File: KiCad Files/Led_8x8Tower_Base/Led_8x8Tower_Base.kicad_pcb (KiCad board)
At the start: 2 copper layers, 160 x 152 mm, 0 parts

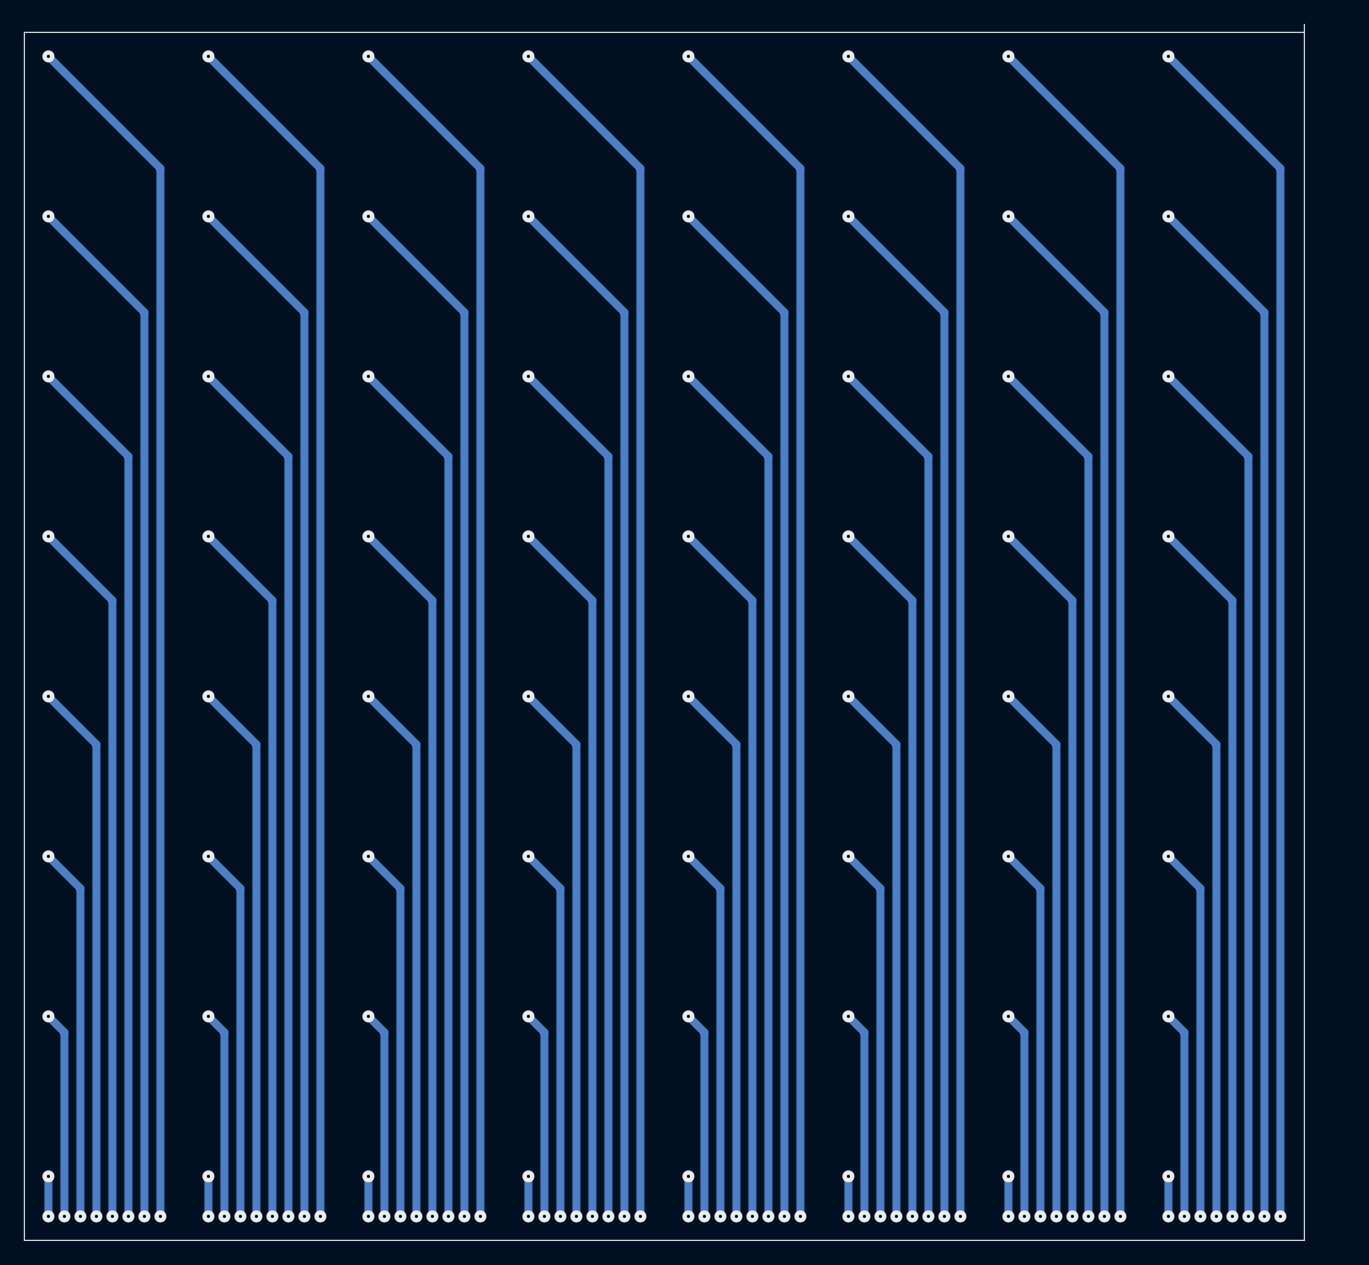
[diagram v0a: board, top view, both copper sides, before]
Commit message: Parellel processing testing files and New circuit designes  uploaded
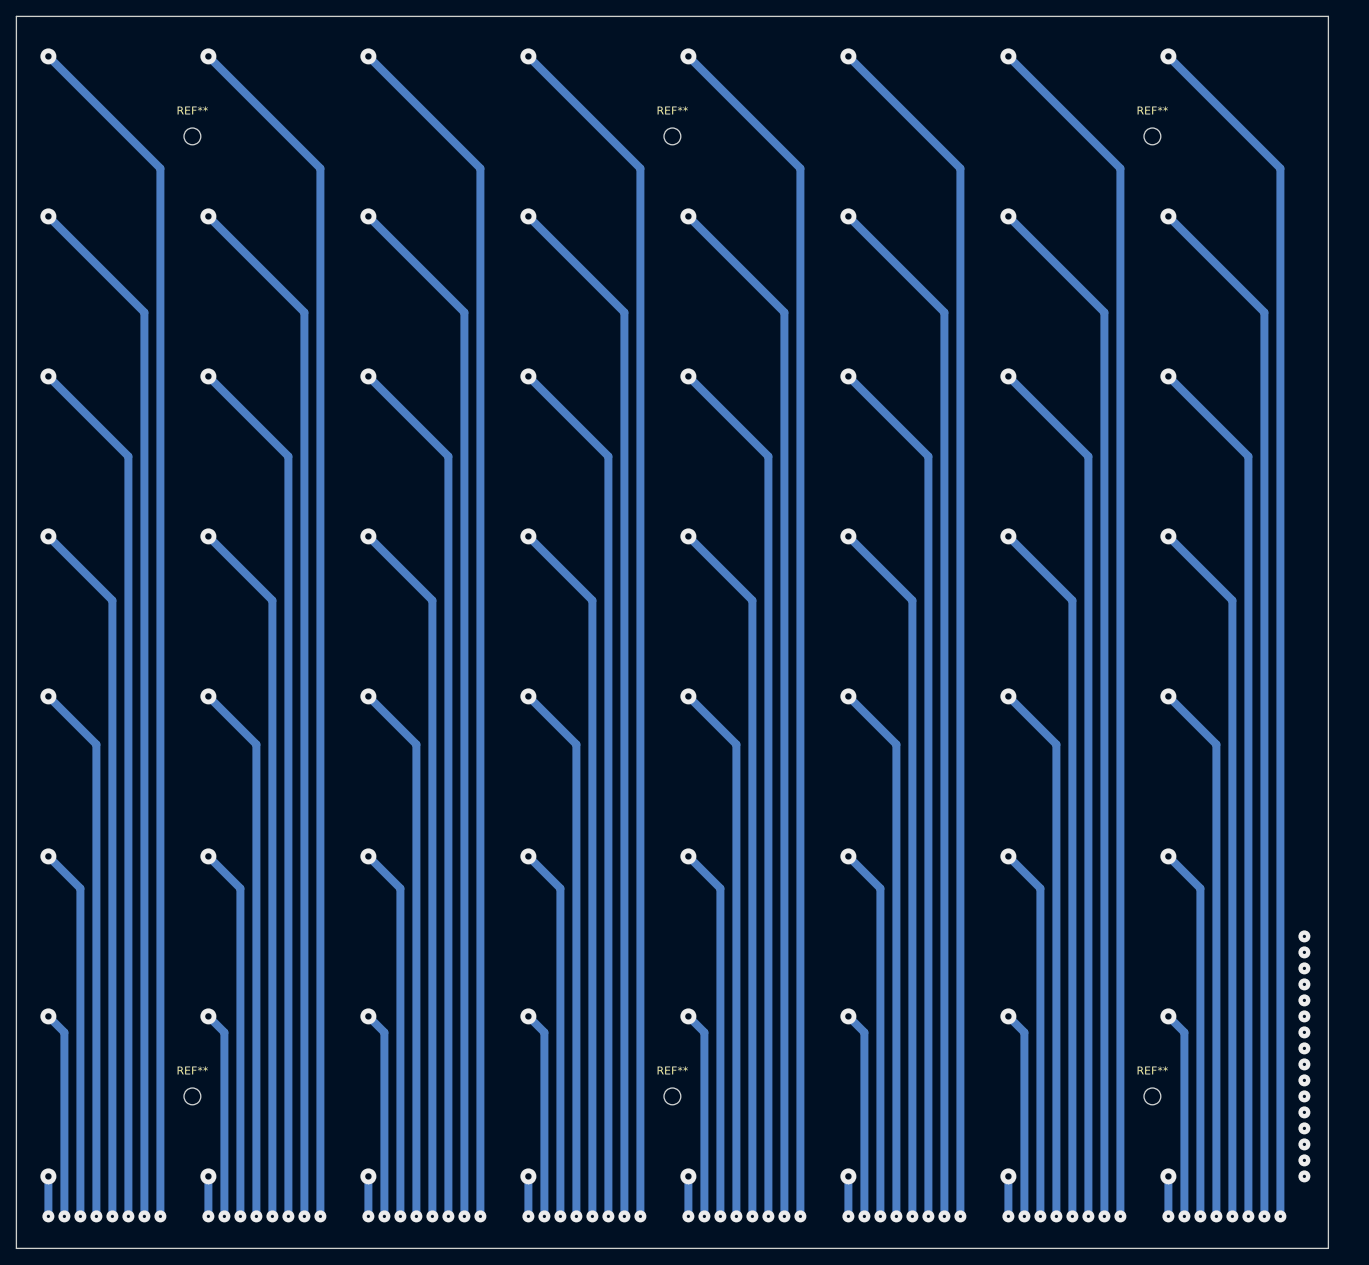
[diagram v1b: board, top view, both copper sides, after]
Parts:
- added REF**: MountingHole_2.1mm, MountingHole:MountingHole_2.1mm, F.Cu at (188.0, 150.0)
- added REF**: MountingHole_2.1mm, MountingHole:MountingHole_2.1mm, F.Cu at (128.0, 30.0)
- added REF**: MountingHole_2.1mm, MountingHole:MountingHole_2.1mm, F.Cu at (128.0, 150.0)
- added REF**: MountingHole_2.1mm, MountingHole:MountingHole_2.1mm, F.Cu at (68.0, 30.0)
- added REF**: MountingHole_2.1mm, MountingHole:MountingHole_2.1mm, F.Cu at (188.0, 30.0)
- added REF**: MountingHole_2.1mm, MountingHole:MountingHole_2.1mm, F.Cu at (68.0, 150.0)
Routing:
- net (no net): vias 128 -> 144
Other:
- board size 160 x 152 mm -> 164 x 154 mm

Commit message: updated files
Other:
- board size 164 x 154 mm -> 167 x 154 mm
